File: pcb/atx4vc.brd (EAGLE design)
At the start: 69.4 x 69 mm, 48 parts, among them IC1 MY_7905DT, J2 ATX24RH

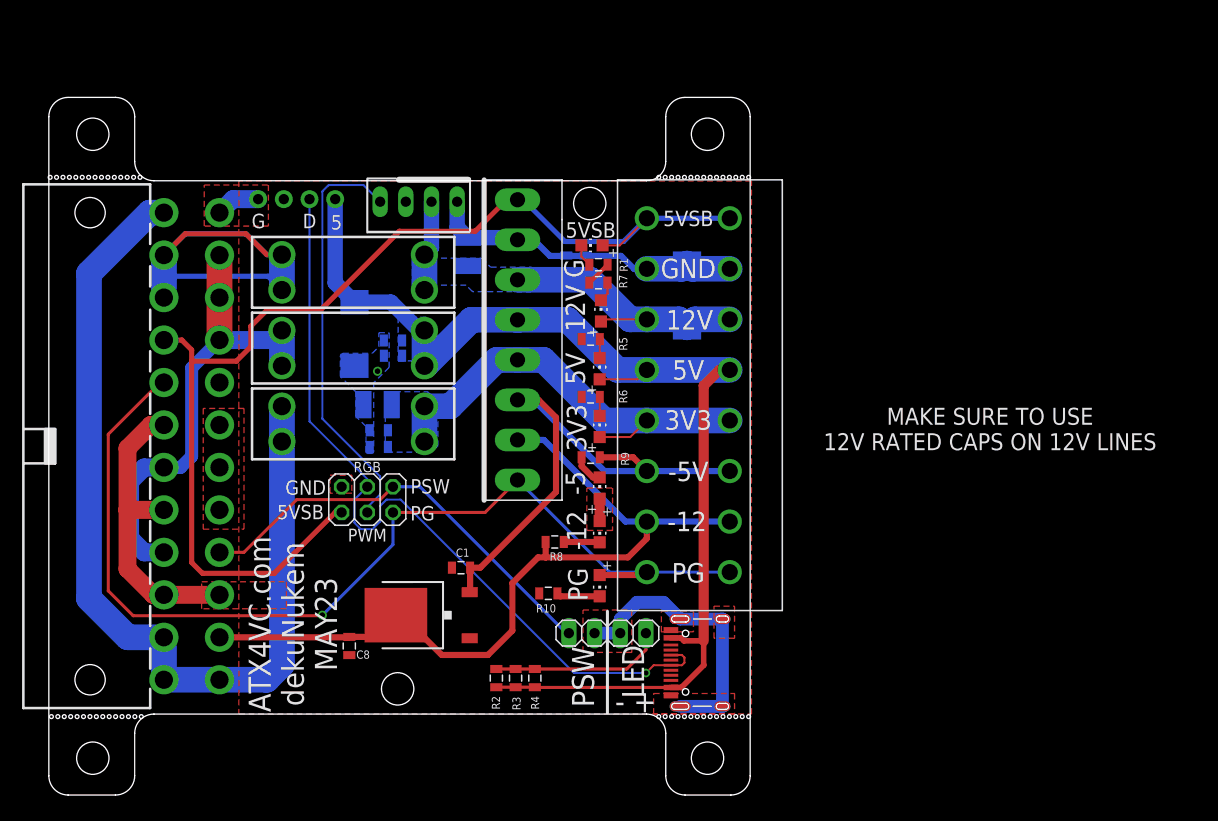
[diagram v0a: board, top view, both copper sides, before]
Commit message: adjust screw location, clean up traces
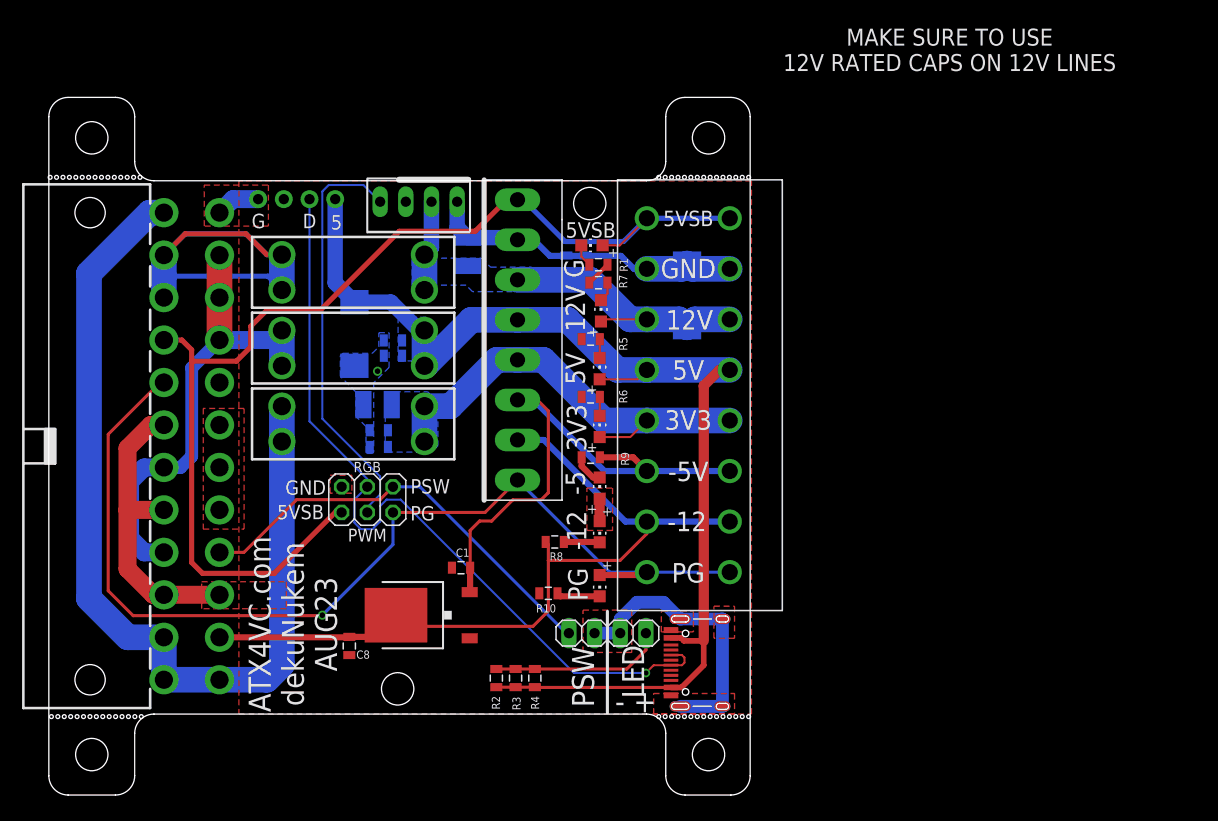
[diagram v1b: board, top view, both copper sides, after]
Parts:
- moved U$5 0.37 mm to (65.2, 65.5)
- moved U$3 0.37 mm to (4.25, 65.5)
- moved U$6 0.37 mm to (65.2, 4.50)
- moved U$4 0.37 mm to (4.25, 4.50)
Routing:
- net -12V: track 79.9 -> 78.4 mm
- net -5V: track 55.0 -> 56.1 mm
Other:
- board text added: "ATX4VC.com dekuNukem AUG23"
- board text removed: "ATX4VC.com dekuNukem MAY23"

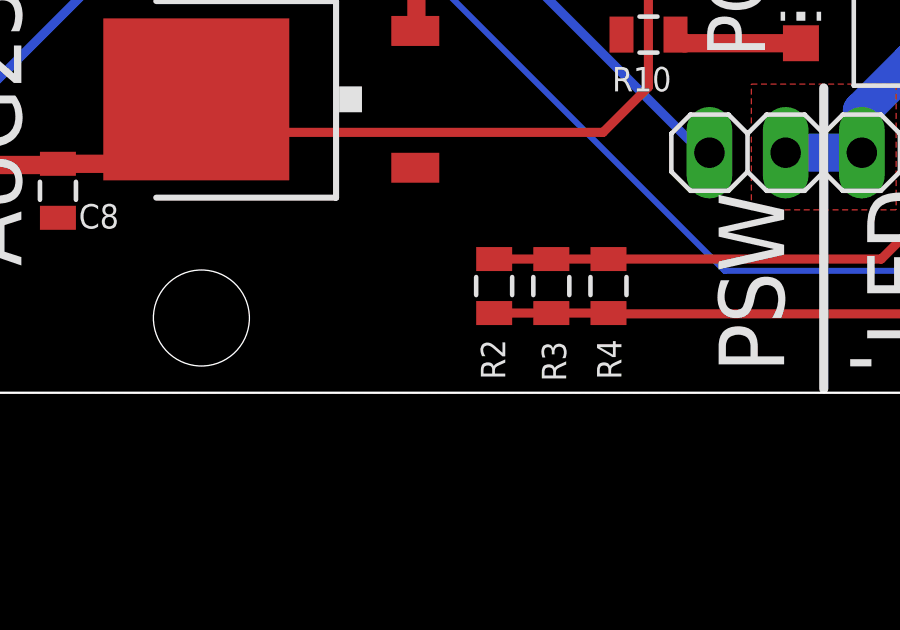
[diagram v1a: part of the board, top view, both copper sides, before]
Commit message: added power LED resistor bypass
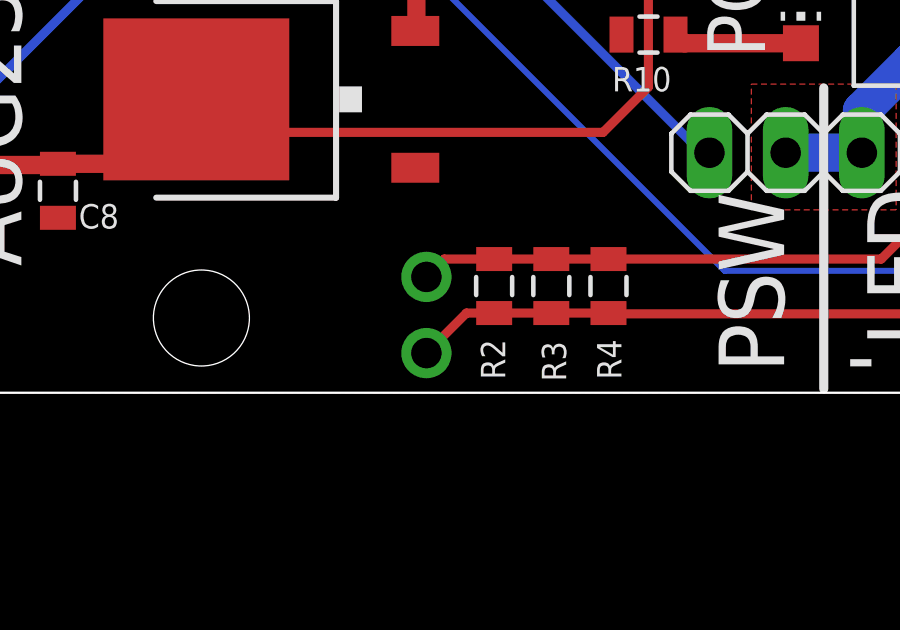
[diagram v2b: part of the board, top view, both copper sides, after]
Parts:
- added U$13: PINHD1X2, adafruit_changed:1X02
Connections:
- net F5V: now also U$13.2
- net N$17: now also U$13.1
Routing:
- net F5V: track 118.0 -> 120.8 mm
- net N$17: track 17.2 -> 19.7 mm
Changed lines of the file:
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@@
 <attribute name="NAME" x="43.307" y="57.023" size="0.8128" layer="26" rot="MR0"/>
 </element>
+<element name="U$13" library="adafruit_changed" package="1X02" value="PINHD1X2" x="42" y="11.1" smashed="yes" rot="R270"/>
 </elements>
 <signals>
@@
 <vertex x="37.338" y="47.752"/>
 </polygon>
+<contactref element="U$13" pad="2"/>
+<wire x1="44.259" y1="11.165" x2="43.335" y2="11.165" width="0.3048" layer="1"/>
+<wire x1="43.335" y1="11.165" x2="42" y2="9.83" width="0.3048" layer="1"/>
 </signal>
 <signal name="F12V">
@@
 <wire x1="59.055" y1="14.859" x2="59.055" y2="16.51" width="0.3048" layer="1"/>
 <wire x1="57.161" y1="12.965" x2="59.055" y2="14.859" width="0.3048" layer="1"/>
+<contactref element="U$13" pad="1"/>
+<wire x1="44.259" y1="12.965" x2="42.595" y2="12.965" width="0.3048" layer="1"/>
+<wire x1="42.595" y1="12.965" x2="42" y2="12.37" width="0.3048" layer="1"/>
 </signal>
 <signal name="N$11">

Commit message: minor adjustments for next production run
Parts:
- added JP1, JP6: JUMPER-SMT_2_NO_NO-SILK, SparkFun-Jumpers:SMT-JUMPER_2_NO_NO-SILK
- added TP1: TPTP12R, testpad:TP12R
- moved C10 0.30 mm to (32.9, 34.9)
- moved C9 0.30 mm to (32.9, 36.6)
- moved C4 0.10 mm to (34.0, 45.6)
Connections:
- new net N$2: J1.A6, J1.B6, JP1.1
- new net N$4: J1.A7, J1.B7, JP6.1, TP1.TP
- net N$7: now also JP1.2, JP6.2; no longer J1.A6, J1.B6
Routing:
- net N$2: track 0.00 -> 9.43 mm, vias 0 -> 1
- net N$4: track 0.00 -> 8.77 mm, vias 0 -> 1
- net N$7: track 79.4 -> 71.2 mm, vias 1 -> 0
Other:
- board text added: "12"
- board text added: "3"
- board text added: "ATX4VC REV3 dekuNukem JAN24"
- board text added: "ATX4VC.com"
- board text added: "DM"
- board text added: "DP"
- board text removed: "-5V"
- board text removed: "ATX4VC.com dekuNukem AUG23"

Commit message: equal dimension
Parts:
- moved C1 0.53 mm to (40.6, 22.5)
- moved C11 0.53 mm to (41.2, 53.7)
- moved C4 0.53 mm to (33.9, 45.1)
- moved C5 0.53 mm to (33.9, 43.4)
- moved LED2 0.53 mm to (54.3, 42.2)
- moved LED6 0.53 mm to (54.3, 30.4)
- moved R1 0.53 mm to (54.2, 52.5)
- moved R3 0.53 mm to (46.0, 11.6)
- moved R4 0.53 mm to (47.9, 11.6)
- moved R5 0.53 mm to (53.4, 45.1)
- moved R6 0.53 mm to (53.4, 39.4)
- moved R7 0.53 mm to (54.2, 50.7)
- moved R9 0.53 mm to (53.4, 33.4)
- moved TP1 0.53 mm to (58.0, 10.4)
- moved U$12 0.53 mm to (63.1, 42.0)
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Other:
- board size 69.4 x 69 mm -> 69 x 69 mm

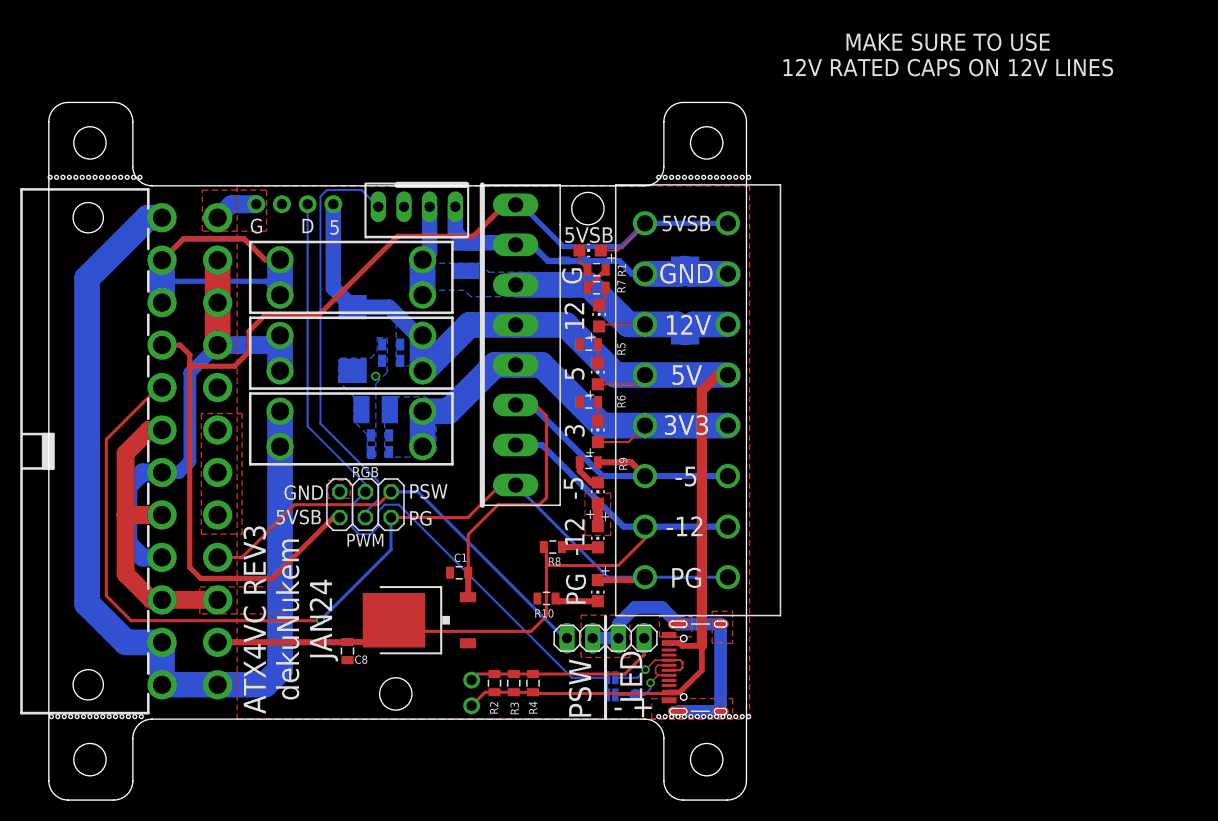
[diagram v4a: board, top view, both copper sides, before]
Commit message: adjusted snapoff holes
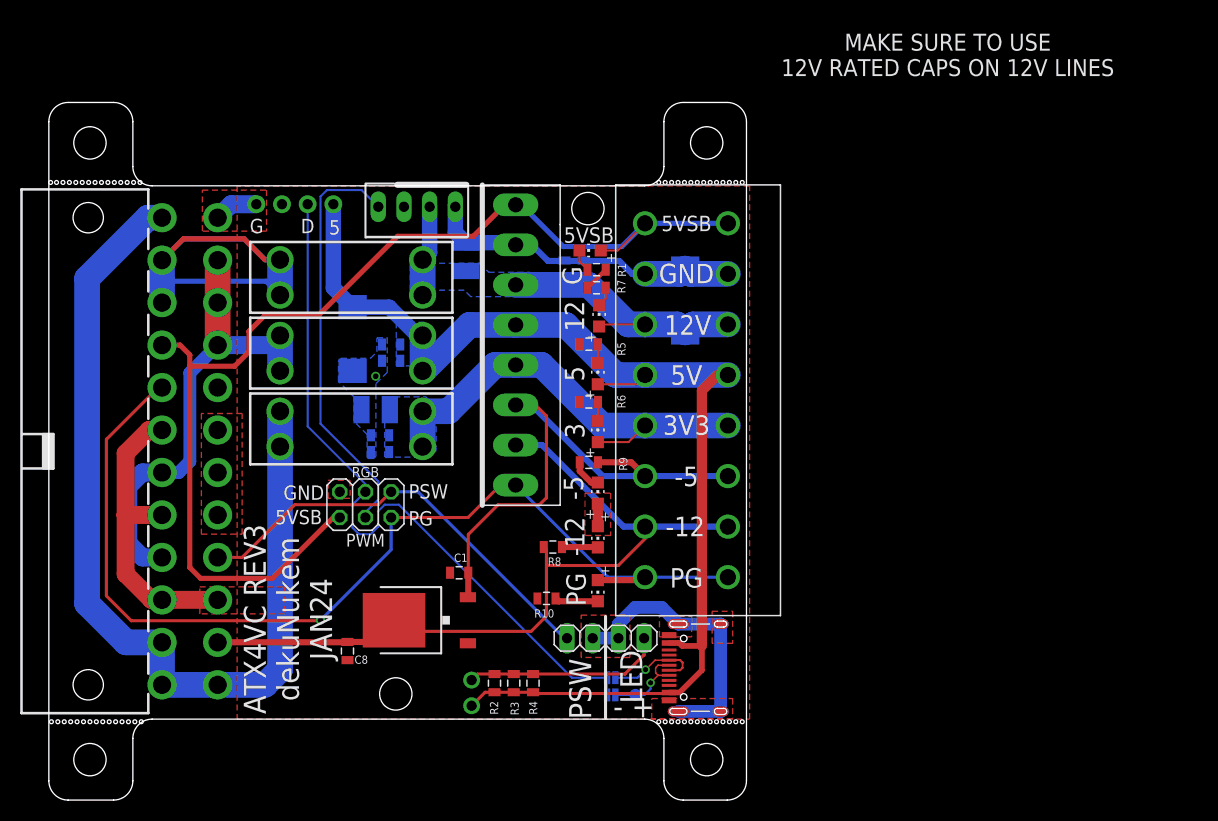
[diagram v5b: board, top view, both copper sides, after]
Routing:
- net -12V: track 78.4 -> 77.8 mm
- net F5V: track 120.9 -> 120.3 mm

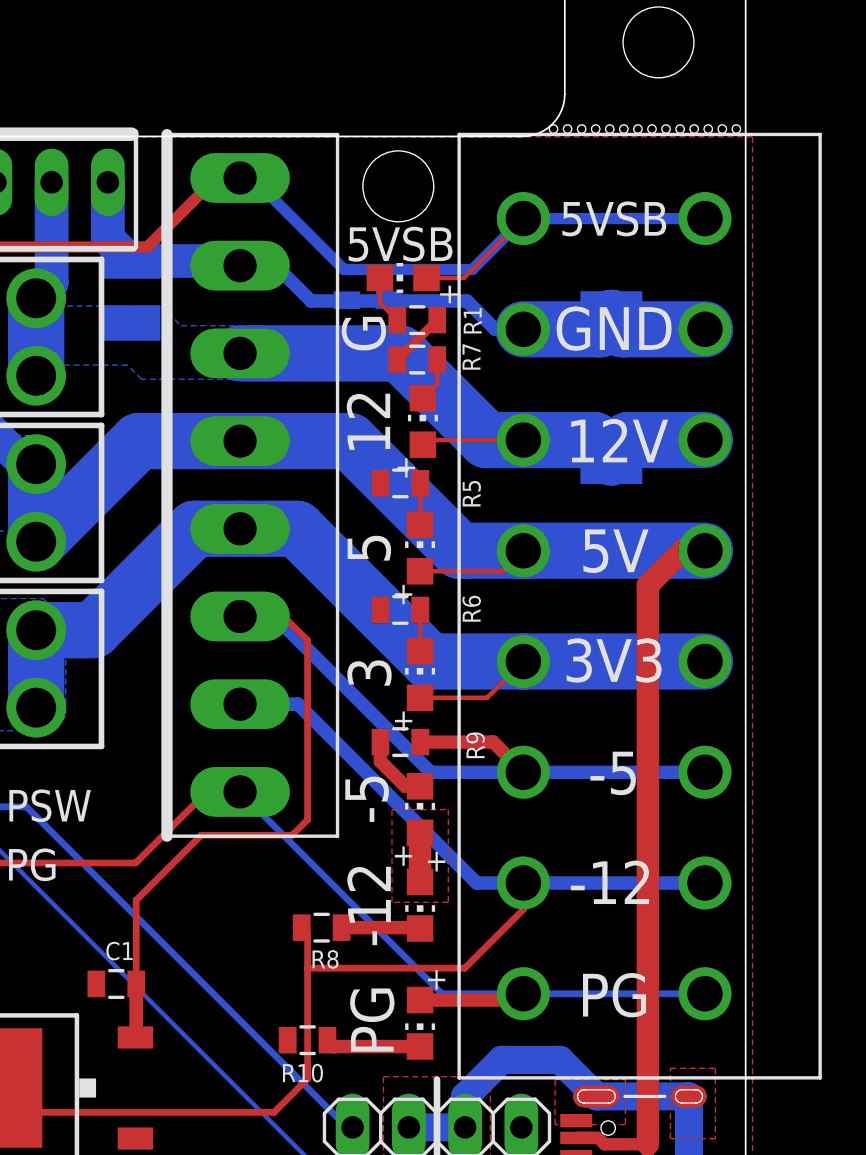
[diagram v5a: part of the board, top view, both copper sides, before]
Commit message: adjusted hole size
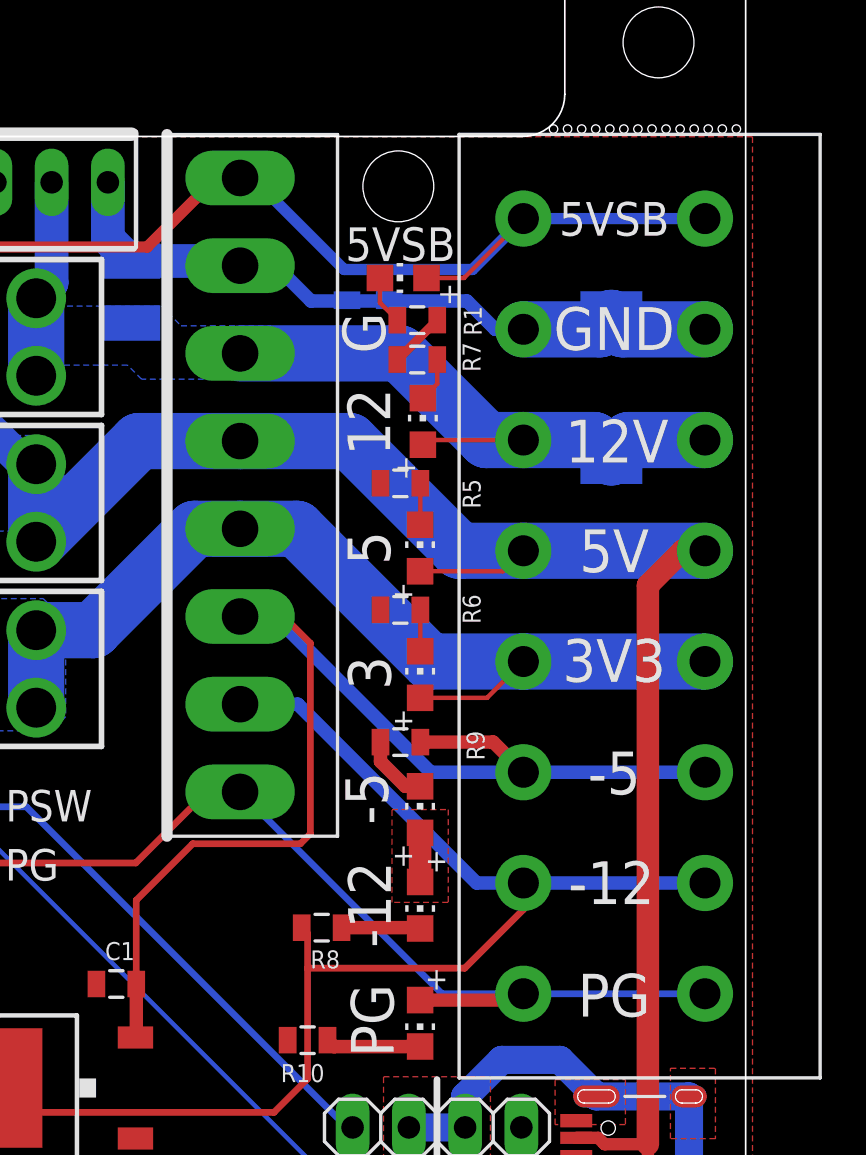
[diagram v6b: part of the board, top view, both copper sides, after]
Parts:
- U$7: value VH396_8P -> 396_CONN_VH396_8P; device 396_conn:396_8P -> atx4vc:396_CONN_396_8P
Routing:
- net -5V: track 56.2 -> 56.7 mm
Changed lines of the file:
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@@
 <setting verticaltext="up"/>
 </settings>
-<grid distance="12.5" unitdist="mil" unit="mil" style="lines" multiple="1" display="no" altdistance="1" altunitdist="mil" altunit="mil"/>
+<grid distance="5" unitdist="mil" unit="mil" style="lines" multiple="1" display="no" altdistance="1" altunitdist="mil" altunit="mil"/>
 <layers>
 <layer number="1" name="Top" color="4" fill="1" visible="yes" active="yes"/>
@@
 <element name="U$10" library="atx_power_control" package="FUSE_HOLDER_3IN1" value="CAR_FUSE_HOLDER3IN1" x="29.9165" y="36.711" smashed="yes"/>
 <element name="U$9" library="atx_power_control" package="FUSE_HOLDER_3IN1" value="CAR_FUSE_HOLDER3IN1" x="29.9165" y="44.204" smashed="yes"/>
-<element name="U$7" library="396_conn" package="396_8P" value="VH396_8P" x="46.1725" y="43.038" smashed="yes" rot="R90"/>
+<element name="U$7" library="atx4vc" package="396_CONN_396_8P" value="396_CONN_VH396_8P" x="46.1725" y="43.038" smashed="yes" rot="R90"/>
 <element name="R2" library="atx_power_control" package="0805" value="5K1" x="44.0765" y="11.565" smashed="yes" rot="R270">
 <attribute name="NAME" x="43.632" y="9.787" size="0.8128" layer="25" rot="R270"/>
@@
 <wire x1="41.4845" y1="20.105" x2="41.4475" y2="20.068" width="0.6096" layer="1"/>
 <wire x1="46.1725" y1="39.078" x2="48.1395" y2="39.078" width="0.3048" layer="1"/>
-<wire x1="48.1395" y1="39.078" x2="49.2175" y2="38" width="0.3048" layer="1"/>
-<wire x1="49.2175" y1="38" x2="49.2175" y2="29.9" width="0.3048" layer="1"/>
-<wire x1="49.2175" y1="29.9" x2="48.5175" y2="29.2" width="0.3048" layer="1"/>
-<wire x1="48.5175" y1="29.2" x2="44.4175" y2="29.2" width="0.3048" layer="1"/>
-<wire x1="44.4175" y1="29.2" x2="41.4845" y2="26.267" width="0.3048" layer="1"/>
+<wire x1="48.1395" y1="39.078" x2="49.3445" y2="37.873" width="0.3048" layer="1"/>
+<wire x1="49.3445" y1="37.873" x2="49.3445" y2="29.265" width="0.3048" layer="1"/>
+<wire x1="49.3445" y1="29.265" x2="48.8985" y2="28.819" width="0.3048" layer="1"/>
+<wire x1="48.8985" y1="28.819" x2="44.0365" y2="28.819" width="0.3048" layer="1"/>
+<wire x1="44.0365" y1="28.819" x2="41.4845" y2="26.267" width="0.3048" layer="1"/>
 <wire x1="41.4845" y1="26.267" x2="41.4845" y2="22.485" width="0.3048" layer="1"/>
 </signal>
